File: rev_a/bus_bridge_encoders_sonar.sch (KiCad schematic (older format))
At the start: 59 parts, among them J1 POWER_SELECT, J2 TERMINATE_JUMPER, SW1 2_LEAD_PUSH_BUTTON, U1 LM2940, U2 LTV-826, U3 LTV-826, U4 LTV-826, U5 754410, U6 LM2940, U7 74HCT08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

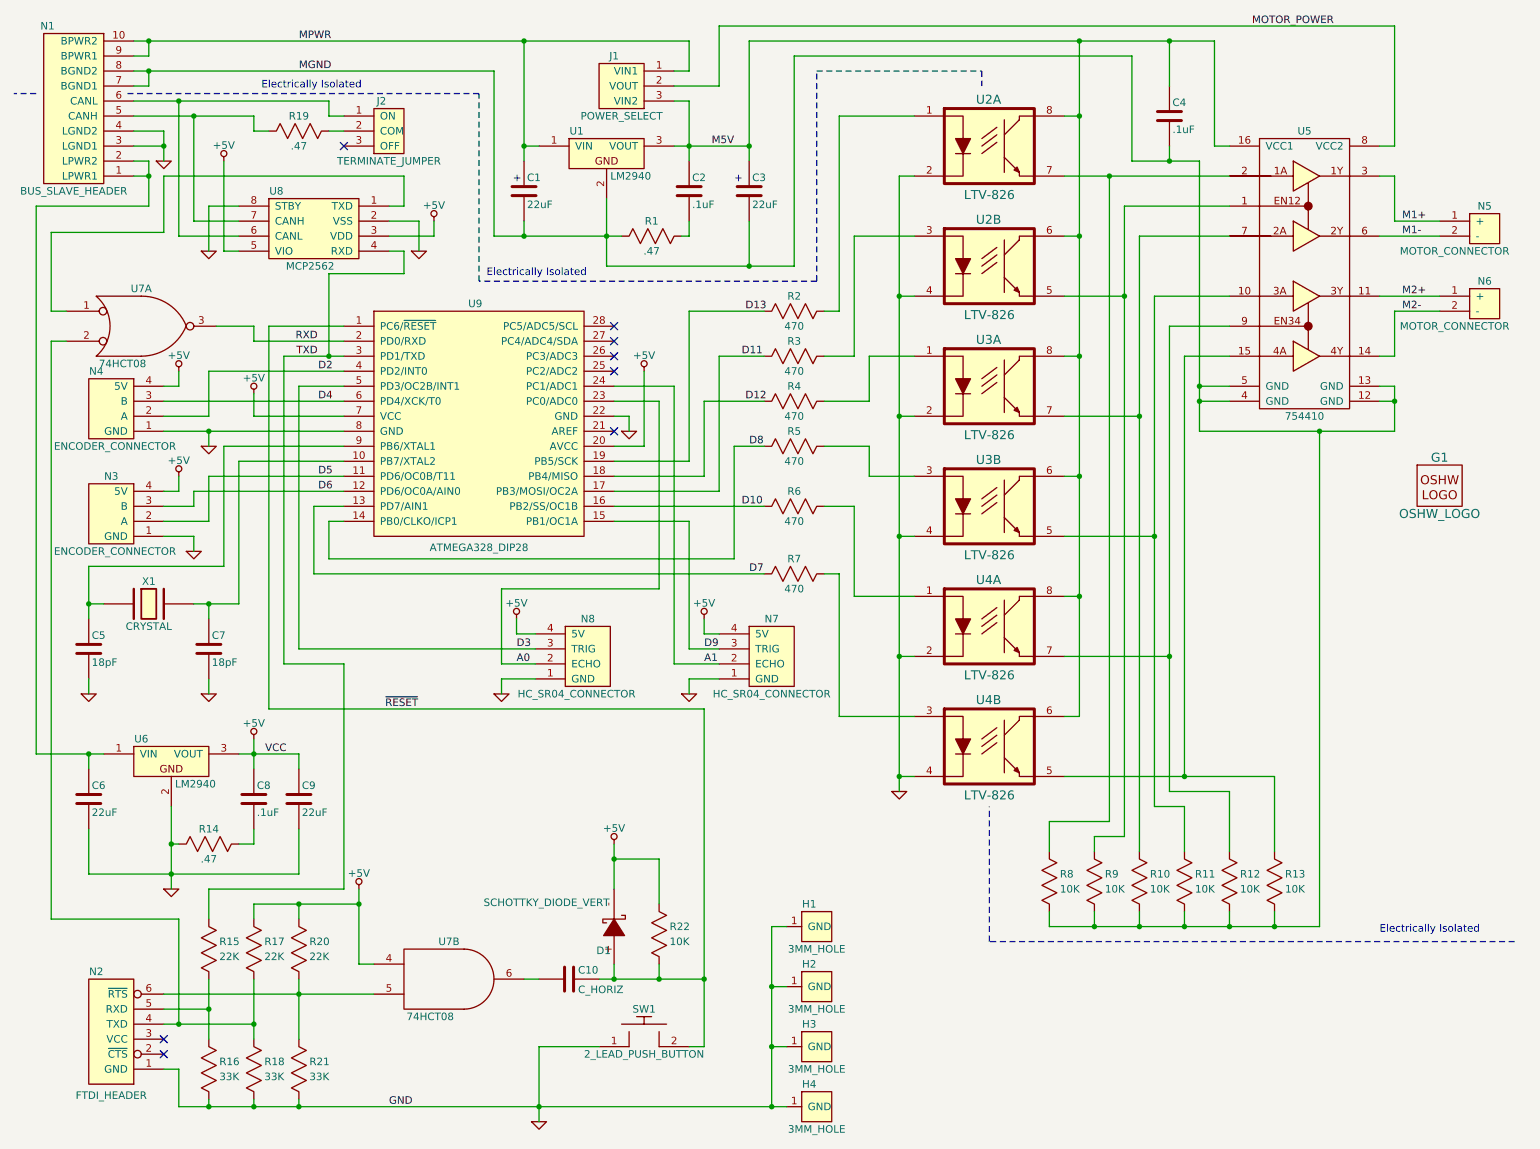
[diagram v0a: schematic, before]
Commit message: Finished Rev. A board layout.
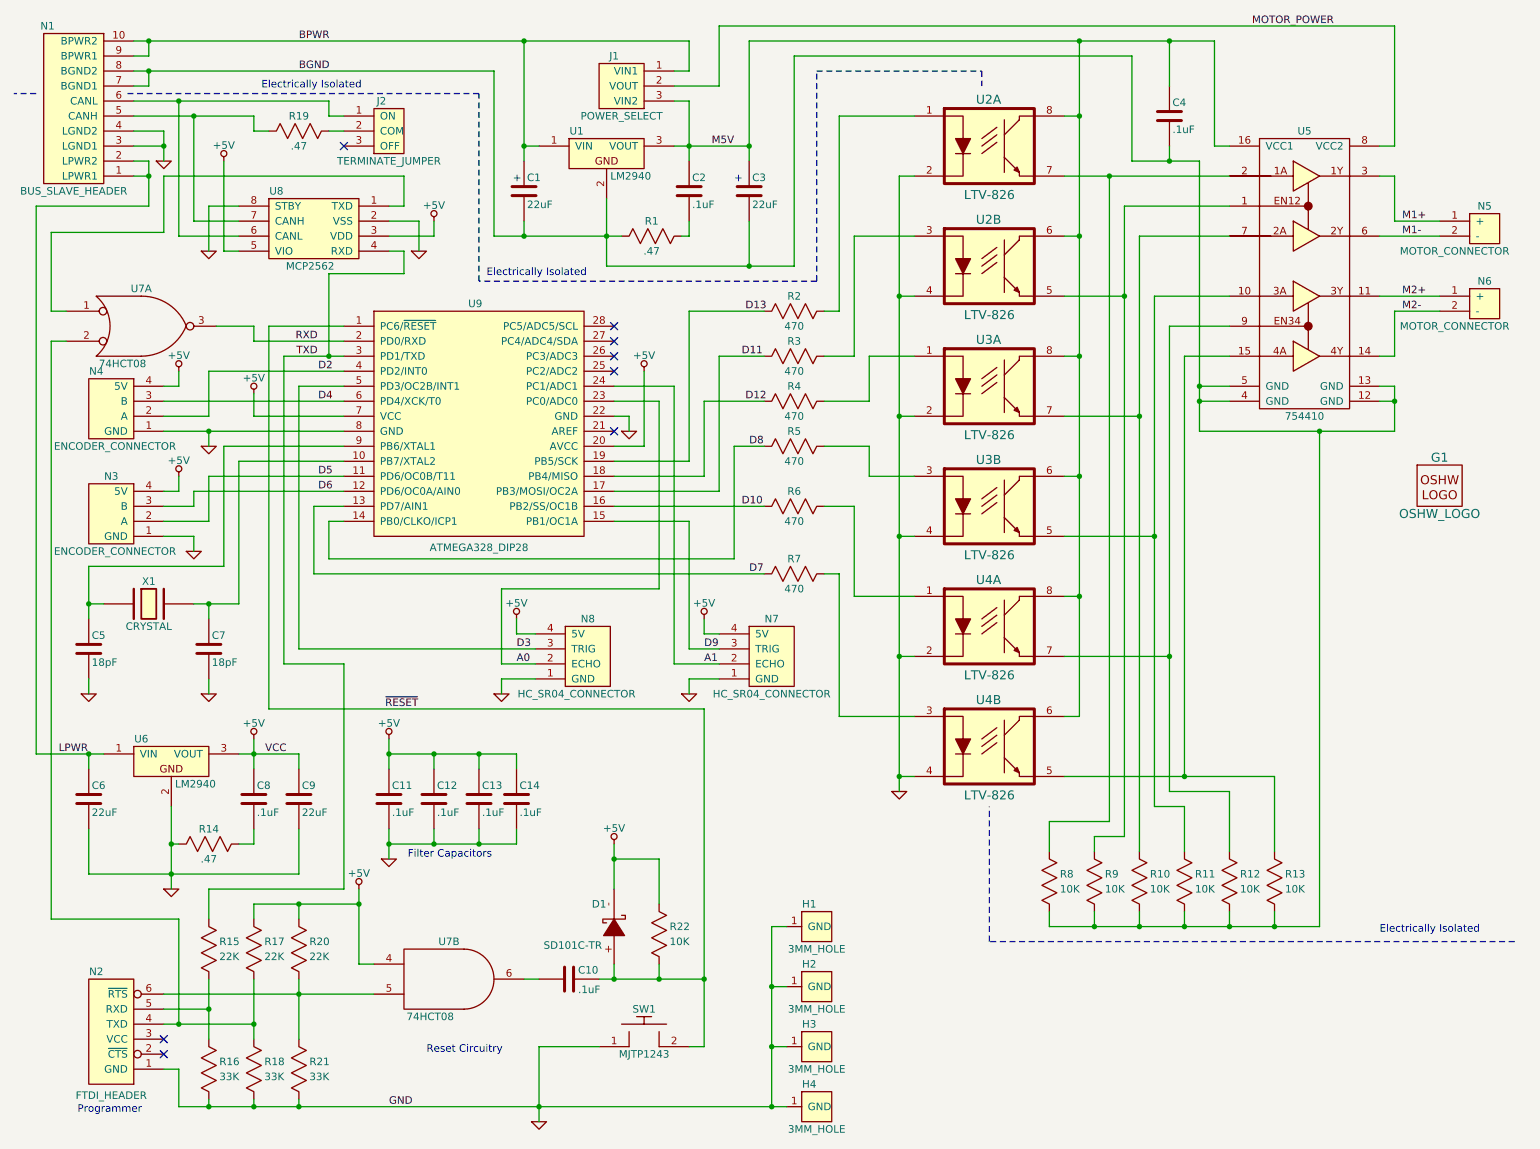
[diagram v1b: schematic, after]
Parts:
- added C11, C12, C13, C14: .1uF, symbol C_VERT
- C10: value C_HORIZ -> .1uF
- D1: value SCHOTTKY_DIODE_VERT -> SD101C-TR
- SW1: value 2_LEAD_PUSH_BUTTON -> MJTP1243
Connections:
- net +5V: now also C11.1, C12.1, C13.1, C14.1
- net GND: now also C11.2, C12.2, C13.2, C14.2
- net LPWR: now reaches C6.1, N1.1 (LPWR1), N1.2 (LPWR2), U6.1 (VIN)
- net MGND renamed BGND
- net MPWR renamed BPWR
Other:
- note added: "Filter Capacitors"
- note added: "Programmer"
- note added: "Reset Circuitry"

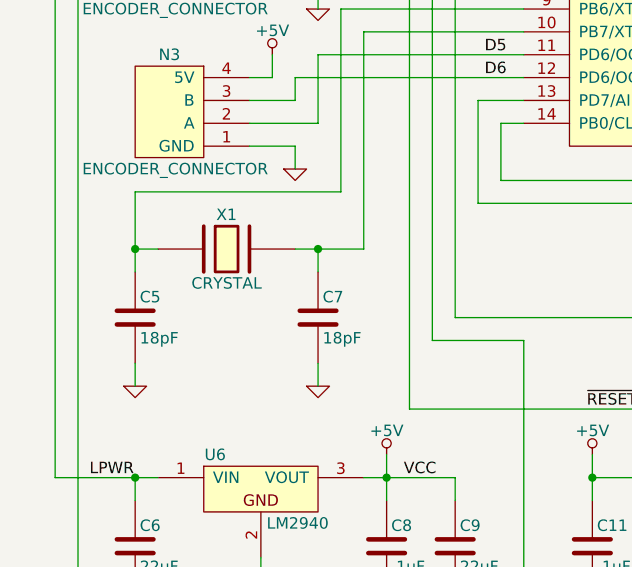
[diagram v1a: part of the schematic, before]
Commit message: CRYSTAL=>16MHz
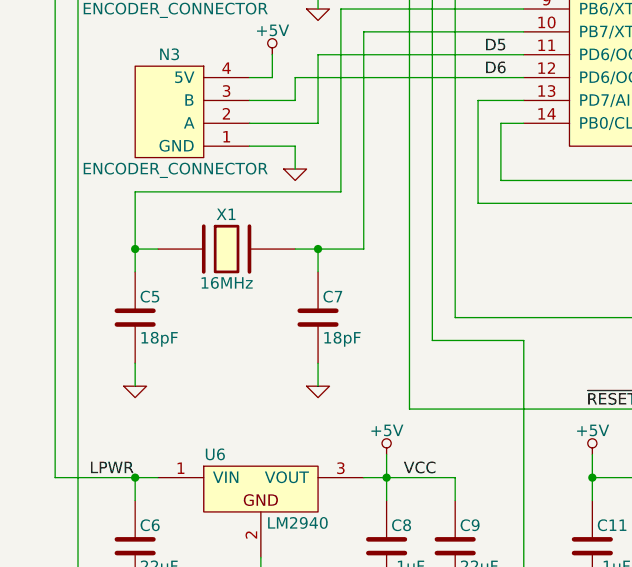
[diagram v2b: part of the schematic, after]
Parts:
- X1: value CRYSTAL -> 16MHz
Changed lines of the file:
@@
 P 1400 4450
 F 0 "X1" H 1400 4600 50  0000 C CNN
-F 1 "CRYSTAL" H 1400 4300 50  0000 C CNN
+F 1 "16MHz" H 1400 4300 50  0000 C CNN
 F 2 "" H 1400 4450 60  0000 C CNN
 F 3 "" H 1400 4450 60  0000 C CNN
